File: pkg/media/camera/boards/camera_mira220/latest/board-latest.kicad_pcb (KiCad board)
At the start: 6 copper layers, 32 x 32 mm, 45 parts, among them J2 FPC, U1 TCR3DF25LM, U2 TCR2EF18LM, U3 TCR2EF135LM, U5 LM3880MF-1AA/NOPB, X2 ECS-2520MV-xxx-xx

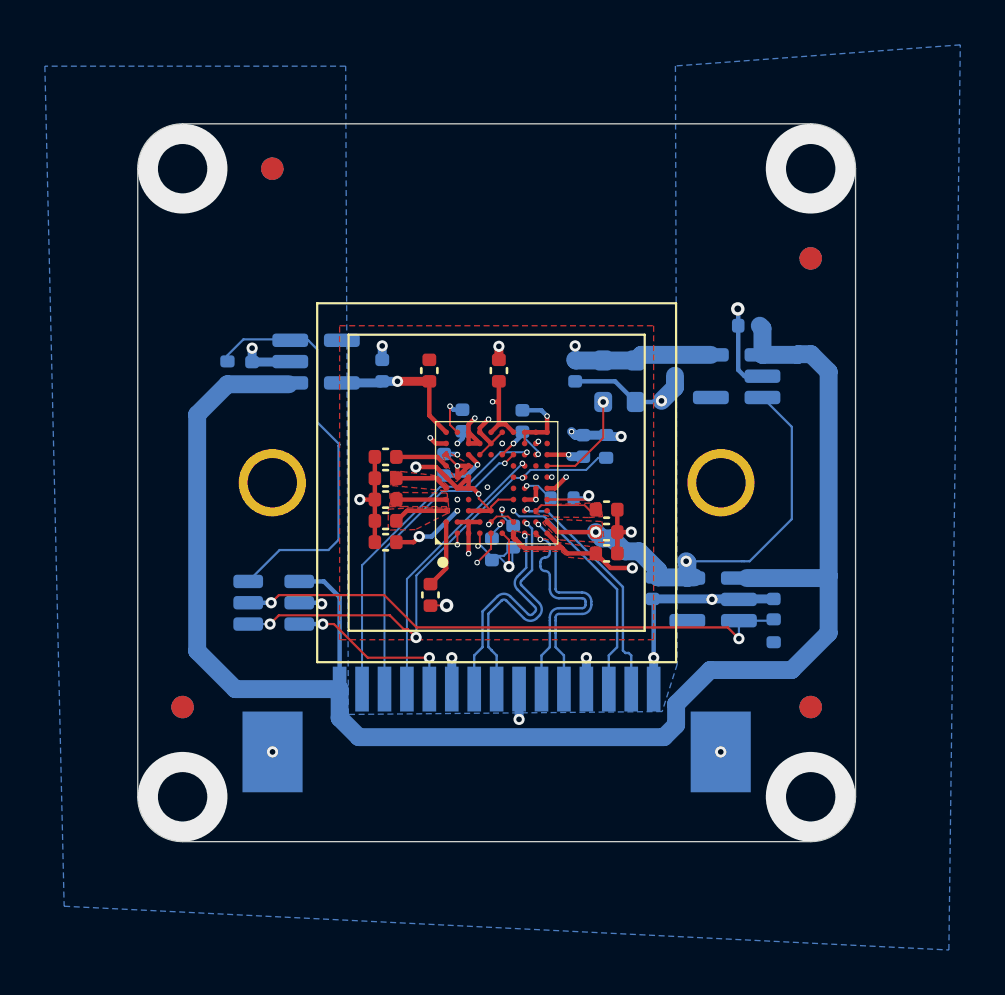
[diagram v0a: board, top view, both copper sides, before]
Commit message: Adding more recent changes and improving licensing.
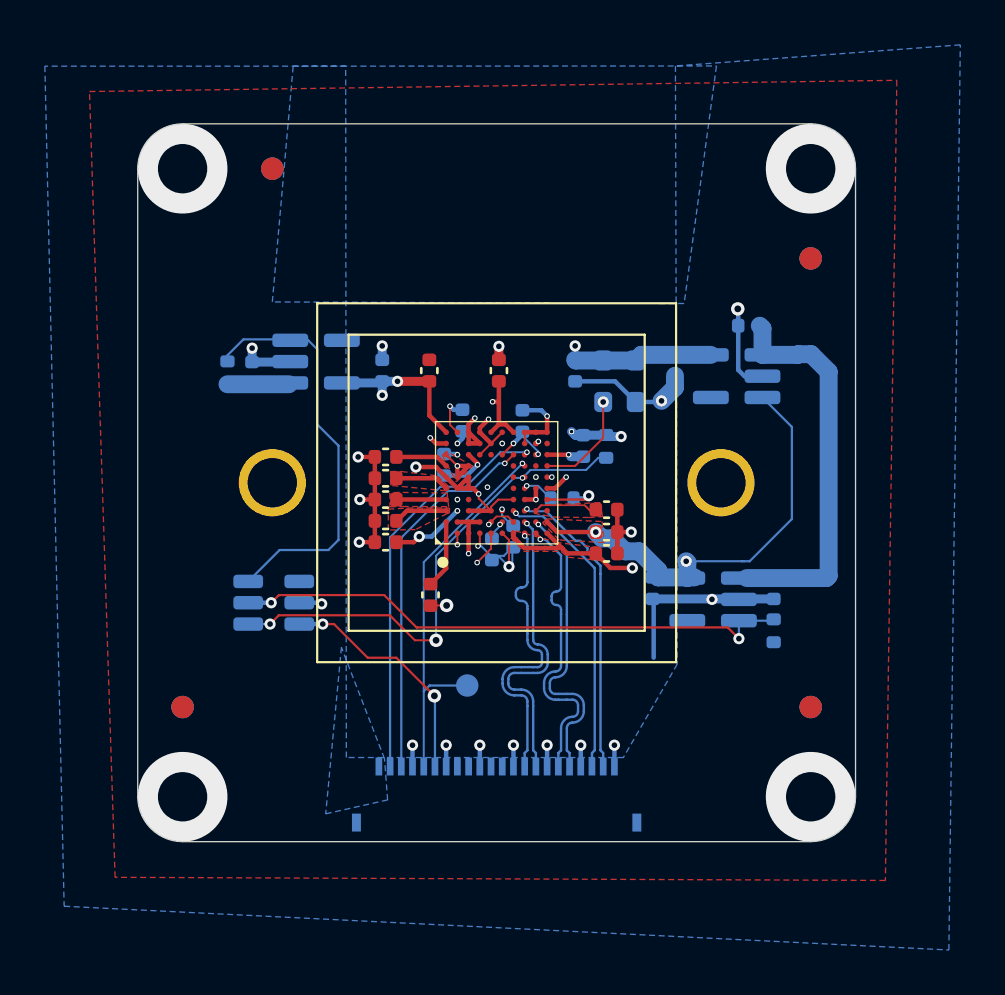
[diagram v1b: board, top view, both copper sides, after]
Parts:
- removed J2: FPC, Connector_FFC-FPC:TE_1-84952-5_1x15-1MP_P1.0mm_Horizontal
- added J1: FH34SRJ-22S-0.5SH_50_, FH34SRJ-22S-0.5SH_50_:HRS_FH34SRJ-22S-0.5SH_50_, B.Cu at (116.0, 129.9)
- added TP1: TRIGGER, TestPoint:TestPoint_Pad_D1.0mm, B.Cu at (114.7, 125.0)
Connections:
- net VDD33 renamed +3V3
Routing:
- net +3V3: track 74.4 -> 20.2 mm
- net /REQ_EXP: track 12.3 -> 17.5 mm
- net /SCK: track 13.7 -> 16.7 mm
- net /SDA: track 15.1 -> 18.0 mm
- net /CAM_ENABLE: track 7.82 -> 10.5 mm
- net GND: track 67.5 -> 70.0 mm, vias 33 -> 36
- net /CON_MIPI_CLK_N: track 11.4 -> 13.6 mm
- net /CON_MIPI_D0_N: track 11.3 -> 13.6 mm
- net /CON_MIPI_D0_P: track 11.4 -> 13.6 mm
- net /CON_MIPI_D1_N: track 11.3 -> 13.5 mm
- net /CON_MIPI_D1_P: track 11.3 -> 13.5 mm
- net /CON_MIPI_CLK_P: track 11.4 -> 13.6 mm
- net /ARST_B: track 21.6 -> 22.3 mm
- net VDD25: track 21.8 -> 22.4 mm, vias 7 -> 8
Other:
- board text added: "MIRA R2"
- board text removed: "MIRA R1"
- board text removed: "TODO: Add more dedicated GND vias per capacitor"
- board text removed: "TODO: More 2.5V vias at the source"

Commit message: Doing some re-organization.
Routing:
- net VDD18: track 17.8 -> 13.3 mm
- net GND: track 70.0 -> 67.3 mm
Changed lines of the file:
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@@
 	)
 	(via
+		(at 124.7 110.3)
+		(size 0.5)
+		(drill 0.25)
+		(layers "F.Cu" "B.Cu")
+		(net 3)
+	)
+	(via
 		(at 119.1 115.75)
 		(size 0.25)
@@
 		(net 3)
 	)
-	(via
-		(at 119.5 109.9)
-		(size 0.5)
-		(drill 0.25)
-		(layers "F.Cu" "B.Cu")
-		(net 3)
-	)
 	(segment
 		(start 119.86 113.88)
@@
 	)
 	(segment
-		(start 119.5 110.52)
-		(end 119.5 109.9)
-		(width 0.2)
+		(start 124.7 110.3)
+		(end 123 110.3)
+		(width 0.8)
 		(layer "B.Cu")
 		(net 3)
@@
 	)
 	(segment
+		(start 123 110.3)
+		(end 122.45 110.3)
+		(width 0.8)
+		(layer "B.Cu")
+		(net 3)
+	)
+	(segment
 		(start 123.98 110.3)
 		(end 123.95 110.27)
@@
 	(segment
 		(start 125.55 110.3)
-		(end 122.45 110.3)
+		(end 124.7 110.3)
 		(width 0.8)
 		(layer "B.Cu")
@@
 	)
 	(segment
-		(start 119.5 113.56)
-		(end 119.34 113.72)
-		(width 0.2)
-		(layer "In3.Cu")
-		(net 3)
-	)
-	(segment
 		(start 117.63 113.93)
 		(end 116.57 113.93)
@@
 	)
 	(segment
-		(start 119.5 109.9)
-		(end 119.5 113.56)
-		(width 0.2)
-		(layer "In3.Cu")
-		(net 3)
-	)
-	(segment
 		(start 119.34 113.72)
 		(end 118.3 113.72)
@@
 	)
 	(segment
-		(start 123 121.38)
-		(end 123 123.8)
-		(width 0.2)
-		(layer "B.Cu")
-		(net 4)
-	)
-	(segment
 		(start 115.17 118.82)
 		(end 115.31 118.82)
@@
 	)
 	(segment
-		(start 123.2 121.18)
-		(end 123 121.38)
-		(width 0.2)
-		(layer "B.Cu")
-		(net 4)
-	)
-	(segment
 		(start 116.7 119.59)
 		(end 116.55 119.74)
@@
 		(polygon
 			(pts
-				(xy 116.075 114.25) (xy 116.125 109.325) (xy 116.325 98.275) (xy 133.925 98.075) (xy 133.63 115.62)
-				(xy 119 116.1) (xy 117.6 114.25) (xy 116.8 114.125) (xy 116.3 114.4)
+				(xy 116.075 114.25) (xy 116.125 109.325) (xy 118.6 109.2) (xy 125.5 109.4) (xy 125.5 115.9) (xy 119 116.1)
+				(xy 117.6 114.25) (xy 116.8 114.125) (xy 116.3 114.4)
 			)
 		)

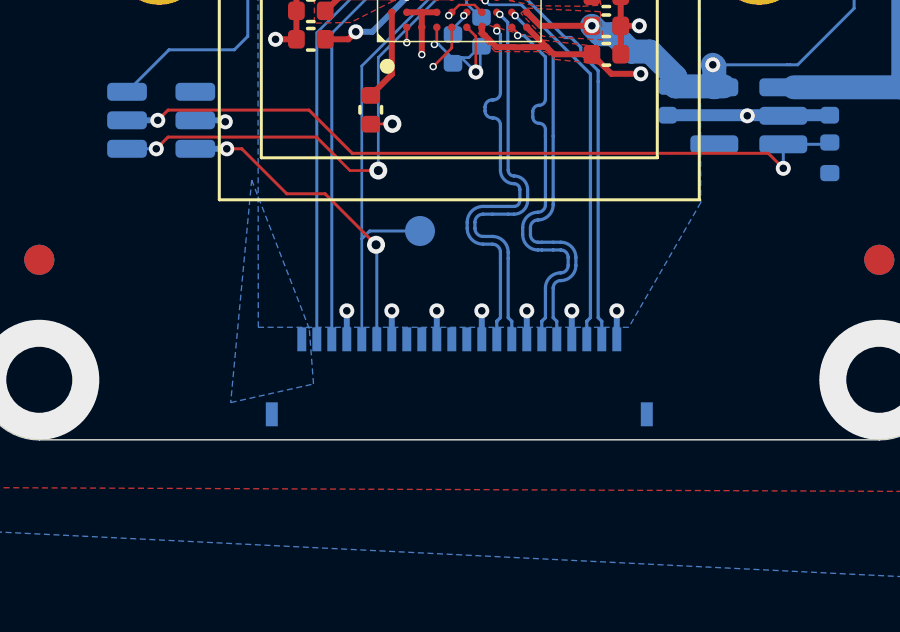
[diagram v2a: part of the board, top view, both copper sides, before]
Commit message: Adding more cnc logging logic.
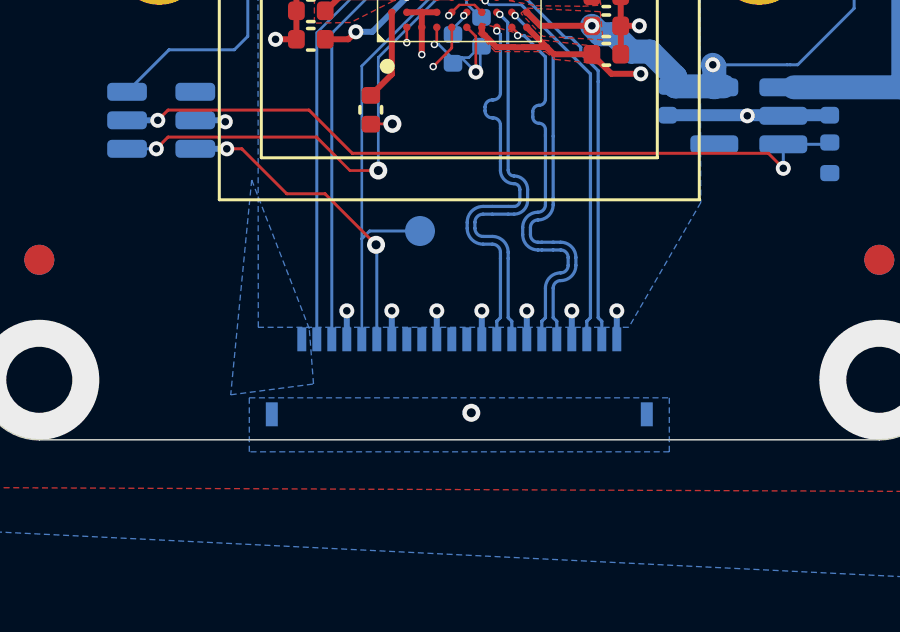
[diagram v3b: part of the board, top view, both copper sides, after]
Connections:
- J1 pad S1: unconnected-(J1-SHIELD-PadS1) -> GND
- J1 pad S2: unconnected-(J1-SHIELD-PadS1)_1 -> GND
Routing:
- net GND: vias 36 -> 37
- added copper zone on B.Cu, net GND
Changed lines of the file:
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@@
 	(net 41 "unconnected-(U2-NC-Pad4)")
 	(net 42 "unconnected-(U3-NC-Pad4)")
-	(net 43 "unconnected-(J1-SHIELD-PadS1)")
-	(net 44 "CM5_MIPI0_D2_N")
-	(net 45 "+3V3")
-	(net 46 "CM5_MIPI0_D3_N")
-	(net 47 "CM5_MIPI0_D3_P")
-	(net 48 "CM5_MIPI0_D2_P")
-	(net 49 "unconnected-(J1-SHIELD-PadS1)_1")
+	(net 43 "CM5_MIPI0_D2_N")
+	(net 44 "+3V3")
+	(net 45 "CM5_MIPI0_D3_N")
+	(net 46 "CM5_MIPI0_D3_P")
+	(net 47 "CM5_MIPI0_D2_P")
 	(footprint "MIRA220ReferenceDesign:MIRA220CSP"
 		(locked yes)
@@
 			(layers "B.Cu" "B.Mask" "B.Paste")
 			(roundrect_rratio 0.25)
-			(net 45 "+3V3")
+			(net 44 "+3V3")
 			(pinfunction "2")
 			(pintype "passive")
@@
 			(layers "B.Cu" "B.Mask" "B.Paste")
 			(roundrect_rratio 0.25)
-			(net 45 "+3V3")
+			(net 44 "+3V3")
 			(pinfunction "1")
 			(pintype "passive")
@@
 			(layers "B.Cu" "B.Mask" "B.Paste")
 			(roundrect_rratio 0.25)
-			(net 45 "+3V3")
+			(net 44 "+3V3")
 			(pinfunction "2")
 			(pintype "passive")
@@
 			(layers "B.Cu" "B.Mask" "B.Paste")
 			(roundrect_rratio 0.25)
-			(net 45 "+3V3")
+			(net 44 "+3V3")
 			(pinfunction "2")
 			(pintype "passive")
@@
 			(layers "B.Cu" "B.Mask" "B.Paste")
 			(roundrect_rratio 0.25)
-			(net 45 "+3V3")
+			(net 44 "+3V3")
 			(pinfunction "1")
 			(pintype "passive")
@@
 			(layers "B.Cu" "B.Mask" "B.Paste")
 			(roundrect_rratio 0.25)
-			(net 45 "+3V3")
+			(net 44 "+3V3")
 			(pinfunction "VIN")
 			(pintype "power_in")
@@
 			(layers "B.Cu" "B.Mask" "B.Paste")
 			(roundrect_rratio 0.25)
-			(net 45 "+3V3")
+			(net 44 "+3V3")
 			(pinfunction "VCC")
 			(pintype "power_in")
@@
 			(size 0.3 0.8)
 			(layers "B.Cu" "B.Mask")
-			(net 45 "+3V3")
+			(net 44 "+3V3")
 			(pinfunction "1")
 			(pintype "passive")
@@
 			(size 0.3 0.8)
 			(layers "B.Cu" "B.Mask")
-			(net 47 "CM5_MIPI0_D3_P")
+			(net 46 "CM5_MIPI0_D3_P")
 			(pinfunction "8")
 			(pintype "passive")
@@
 			(size 0.3 0.8)
 			(layers "B.Cu" "B.Mask")
-			(net 46 "CM5_MIPI0_D3_N")
+			(net 45 "CM5_MIPI0_D3_N")
 			(pinfunction "9")
 			(pintype "passive")
@@
 			(size 0.3 0.8)
 			(layers "B.Cu" "B.Mask")
-			(net 48 "CM5_MIPI0_D2_P")
+			(net 47 "CM5_MIPI0_D2_P")
 			(pinfunction "11")
 			(pintype "passive")
@@
 			(size 0.3 0.8)
 			(layers "B.Cu" "B.Mask")
-			(net 44 "CM5_MIPI0_D2_N")
+			(net 43 "CM5_MIPI0_D2_N")
 			(pinfunction "12")
 			(pintype "passive")
@@
 			(size 0.4 0.8)
 			(layers "B.Cu" "B.Mask" "B.Paste")
-			(net 43 "unconnected-(J1-SHIELD-PadS1)")
+			(net 4 "GND")
 			(pinfunction "SHIELD")
-			(pintype "passive+no_connect")
+			(pintype "passive")
 			(solder_mask_margin 0)
 		)
@@
 			(size 0.4 0.8)
 			(layers "B.Cu" "B.Mask" "B.Paste")
-			(net 49 "unconnected-(J1-SHIELD-PadS1)_1")
+			(net 4 "GND")
 			(pinfunction "SHIELD")
-			(pintype "passive+no_connect")
+			(pintype "passive")
 			(solder_mask_margin 0)
 		)
@@
 			(layers "B.Cu" "B.Mask" "B.Paste")
 			(roundrect_rratio 0.25)
-			(net 45 "+3V3")
+			(net 44 "+3V3")
 			(pinfunction "VIN")
 			(pintype "power_in")
@@
 			(layers "B.Cu" "B.Mask" "B.Paste")
 			(roundrect_rratio 0.25)
-			(net 45 "+3V3")
+			(net 44 "+3V3")
 			(pinfunction "VIN")
 			(pintype "power_in")
@@
 	)
 	(via
+		(at 116.4 131.1)
+		(size 0.6)
+		(drill 0.3)
+		(layers "F.Cu" "B.Cu")
+		(free yes)
+		(net 4)
+	)
+	(via
 		(at 105.1 110)
 		(size 0.5)
@@
 		(width 0.8)
 		(layer "B.Cu")
-		(net 45)
+		(net 44)
 	)
 	(segment
@@
 		(width 0.8)
 		(layer "B.Cu")
-		(net 45)
+		(net 44)
 	)
 	(segment
@@
 		(width 0.8)
 		(layer "B.Cu")
-		(net 45)
+		(net 44)
 	)
 	(segment
@@
 		(width 0.8)
 		(layer "B.Cu")
-		(net 45)
+		(net 44)
 	)
 	(segment
@@
 		(width 0.8)
 		(layer "B.Cu")
-		(net 45)
+		(net 44)
 	)
 	(segment
@@
 		(width 0.8)
 		(layer "B.Cu")
-		(net 45)
+		(net 44)
 	)
 	(segment
@@
 		(width 0.2)
 		(layer "B.Cu")
-		(net 45)
+		(net 44)
 	)
 	(segment
@@
 		(width 0.8)
 		(layer "B.Cu")
-		(net 45)
+		(net 44)
 	)
 	(segment
@@
 		(width 0.8)
 		(layer "B.Cu")
-		(net 45)
+		(net 44)
 	)
 	(segment
@@
 		(width 0.8)
 		(layer "B.Cu")
-		(net 45)
+		(net 44)
 	)
 	(segment
@@
 		(width 0.8)
 		(layer "B.Cu")
-		(net 45)
+		(net 44)
 	)
 	(zone
@@
 	)
 	(zone
-		(net 45)
+		(net 44)
 		(net_name "+3V3")
 		(layer "B.Cu")
@@
 	)
 	(zone
-		(net 45)
+		(net 44)
 		(net_name "+3V3")
 		(layer "B.Cu")
@@
 		(polygon
 			(pts
-				(xy 111 128.3) (xy 109.08 123.34) (xy 108.38 130.76) (xy 111.14 130.14)
+				(xy 111 128.3) (xy 109.08 123.34) (xy 108.38 130.5) (xy 111.14 130.14)
 			)
 		)
 	)
 	(zone
-		(net 45)
+		(net 44)
 		(net_name "+3V3")
 		(layer "B.Cu")
@@
 			)
 		)
+	)
+	(zone
+		(net 4)
+		(net_name "GND")
+		(layer "B.Cu")
+		(hatch edge 0.5)
+		(priority 18)
+		(connect_pads yes
+			(clearance 0.1)
+		)
+		(min_thickness 0.25)
+		(filled_areas_thickness no)
+		(fill yes
+			(thermal_gap 0.5)
+			(thermal_bridge_width 0.5)
+		)
+		(polygon
+			(pts
+				(xy 109 130.6) (xy 123 130.6) (xy 123 132.4) (xy 109 132.4)
+			)
+		)

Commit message: Mocap tweaks and add CM4 support with SDCard.
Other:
- board text added: "TODO: Expose a strobe output debug point."
- board text added: "TODO: Isolate the 2.5V plane from the other supplies."
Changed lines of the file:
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@@
 				(layer "B.Cu"
 					(shape circle)
-					(size 5 5)
+					(size 4 4)
 					(zone_connect -1)
 				)
@@
 				(layer "B.Cu"
 					(shape circle)
-					(size 5 5)
+					(size 4 4)
 					(zone_connect -1)
 				)
@@
 		(layer "Cmts.User")
 		(effects
+			(font
+				(size 1 1)
+				(thickness 0.15)
+			)
+			(justify left bottom)
+		)
+	)
+	(gr_text "TODO: Isolate the 2.5V plane from the other supplies."
+		(at 98.23 92.49 0)
+		(layer "Cmts.User")
+		(effects
+			(font
+				(size 1 1)
+				(thickness 0.15)
+			)
+			(justify left bottom)
+		)
+	)
+	(gr_text "TODO: Expose a strobe output debug point."
+		(at 99.07 89.7 0)
+		(layer "Cmts.User")
+		(effects
